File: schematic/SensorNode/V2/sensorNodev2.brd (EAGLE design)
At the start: 55.9 x 78.7 mm, 30 parts, among them IC1 V_REG_LD1117VXX, U1 ATMEGA328P_PDIP

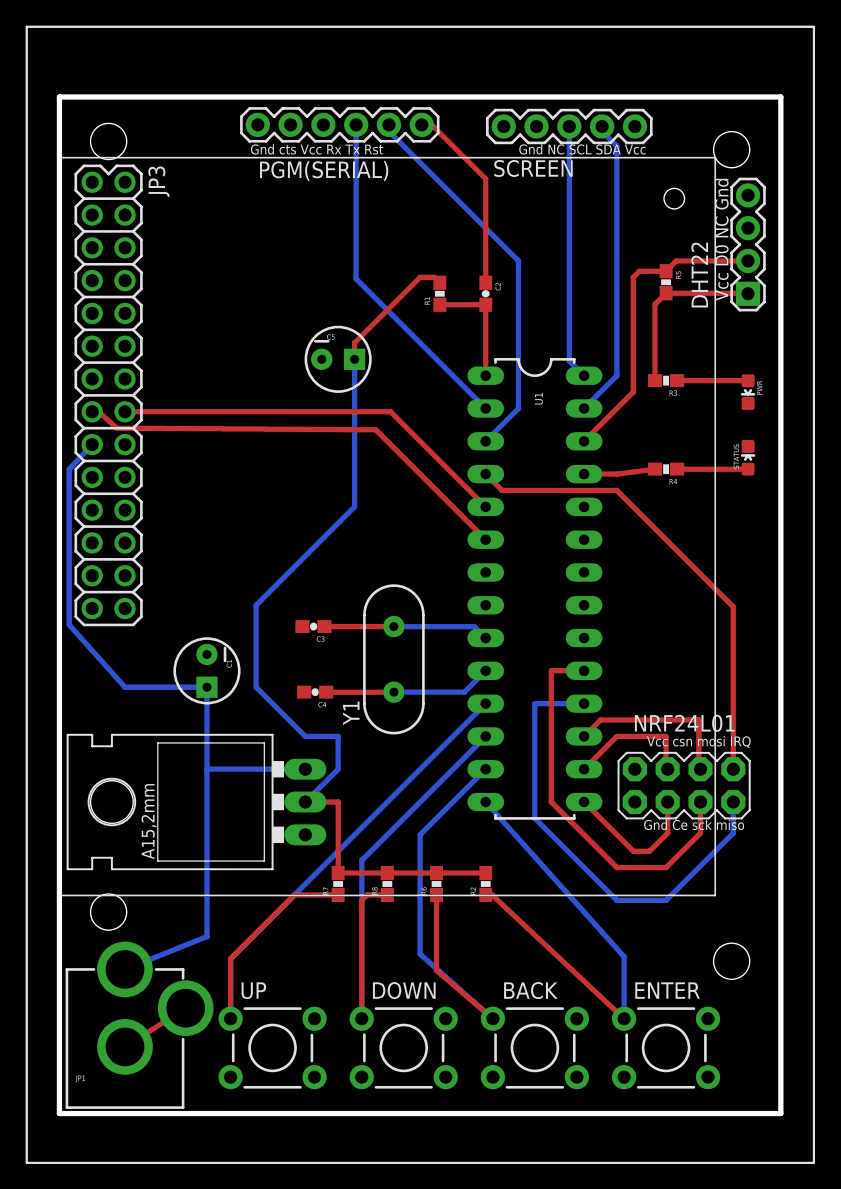
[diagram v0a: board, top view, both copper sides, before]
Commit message: Updating sensor node and gateway node schematics
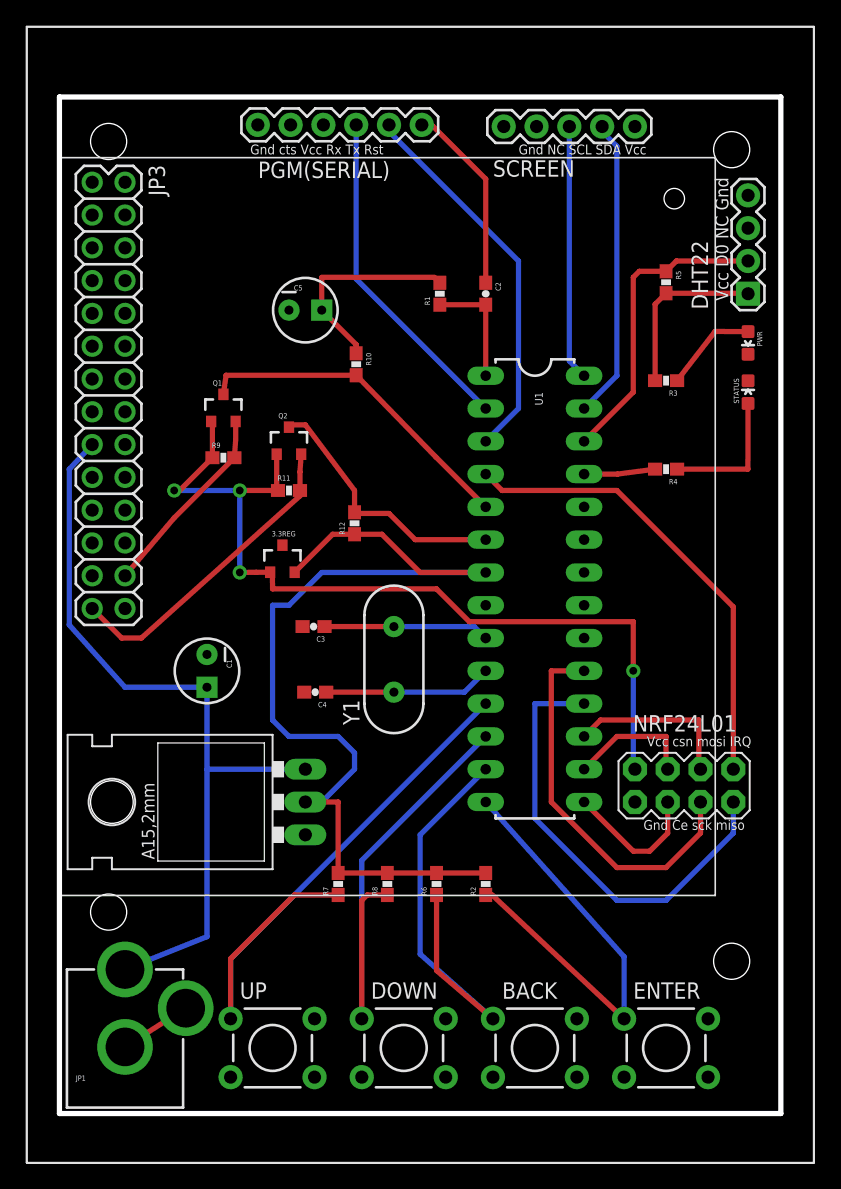
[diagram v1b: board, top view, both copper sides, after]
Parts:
- added 3.3REG: LM3480IM4, SparkFun-PowerIC:SOT23-3
- added Q1, Q2: BSS138, SparkFun:SOT23-3
- added R10, R11, R12, R9: 10K, SparkFun:0603-RES
- moved STATUS 5.08 mm to (53.3, 55.9)
- moved C5 4.58 mm to (19.1, 62.2)
- moved PWR 3.81 mm to (53.3, 59.7)
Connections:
- removed net RX_K30: JP3.16, U1.5
- removed net TX_K30: JP3.15, U1.6
- new net 3V: 3.3REG.1, NRF24L01.2, Q1.1, Q2.1, R11.1, R9.1
- new net RX_K30_H: Q1.3, R10.2, U1.5
- new net RX_K30_L: JP3.26, Q1.2, R9.2
- new net TX_K30_H: Q2.3, R12.2, U1.6
- new net TX_K30_L: JP3.27, Q2.2, R11.2
- net GND: now also 3.3REG.3
- net VCC: now also 3.3REG.2, R10.1, R12.1; no longer NRF24L01.2
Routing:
- net 3V: track 0.00 -> 68.4 mm, vias 0 -> 4
- net TX_K30: track 34.5 -> 0.00 mm
- net RX_K30: track 31.0 -> 0.00 mm
- net RX_K30_H: track 0.00 -> 25.9 mm
- net TX_K30_L: track 0.00 -> 24.5 mm
- net VCC: track 85.7 -> 106.5 mm
- net TX_K30_H: track 0.00 -> 20.8 mm
- net RX_K30_L: track 0.00 -> 15.3 mm
- net N$5: track 5.50 -> 10.6 mm
- net N$4: track 5.50 -> 7.37 mm
